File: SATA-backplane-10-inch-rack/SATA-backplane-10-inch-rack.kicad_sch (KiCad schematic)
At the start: 19 parts, among them J101 Conn_01x06, Q101 DMG1012UW, Q102 DMG1012UW, U1 NCP1117-3.3_SOT223

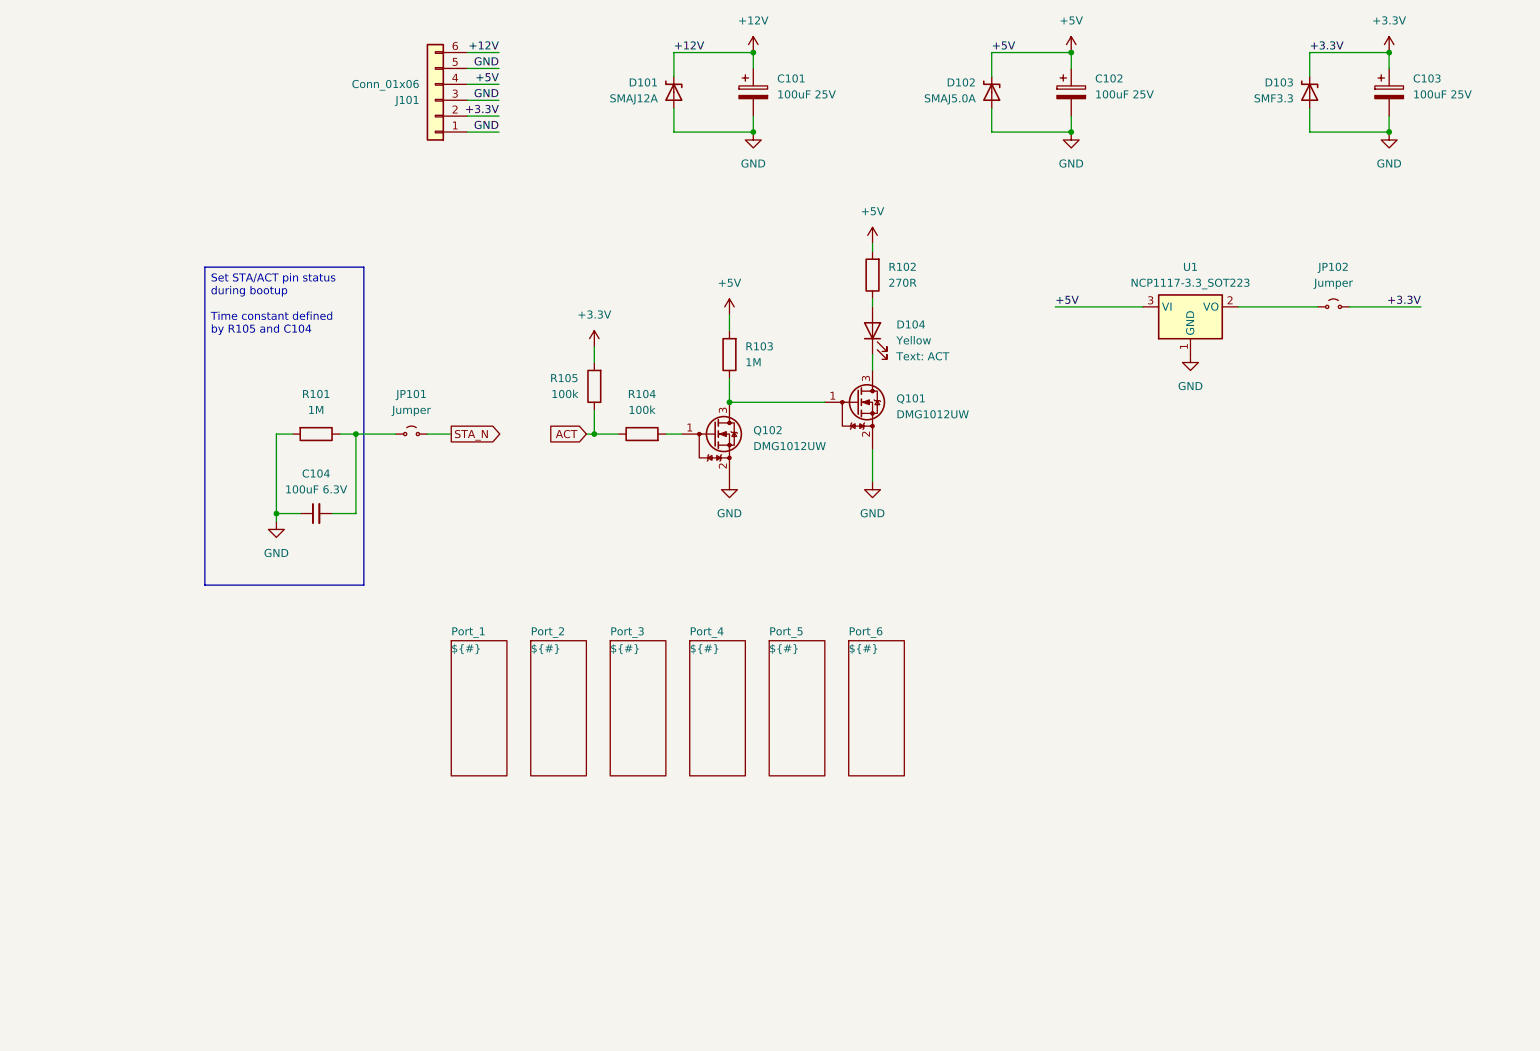
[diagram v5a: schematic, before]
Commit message: Rearrange reference designators numbering and silkscreen items
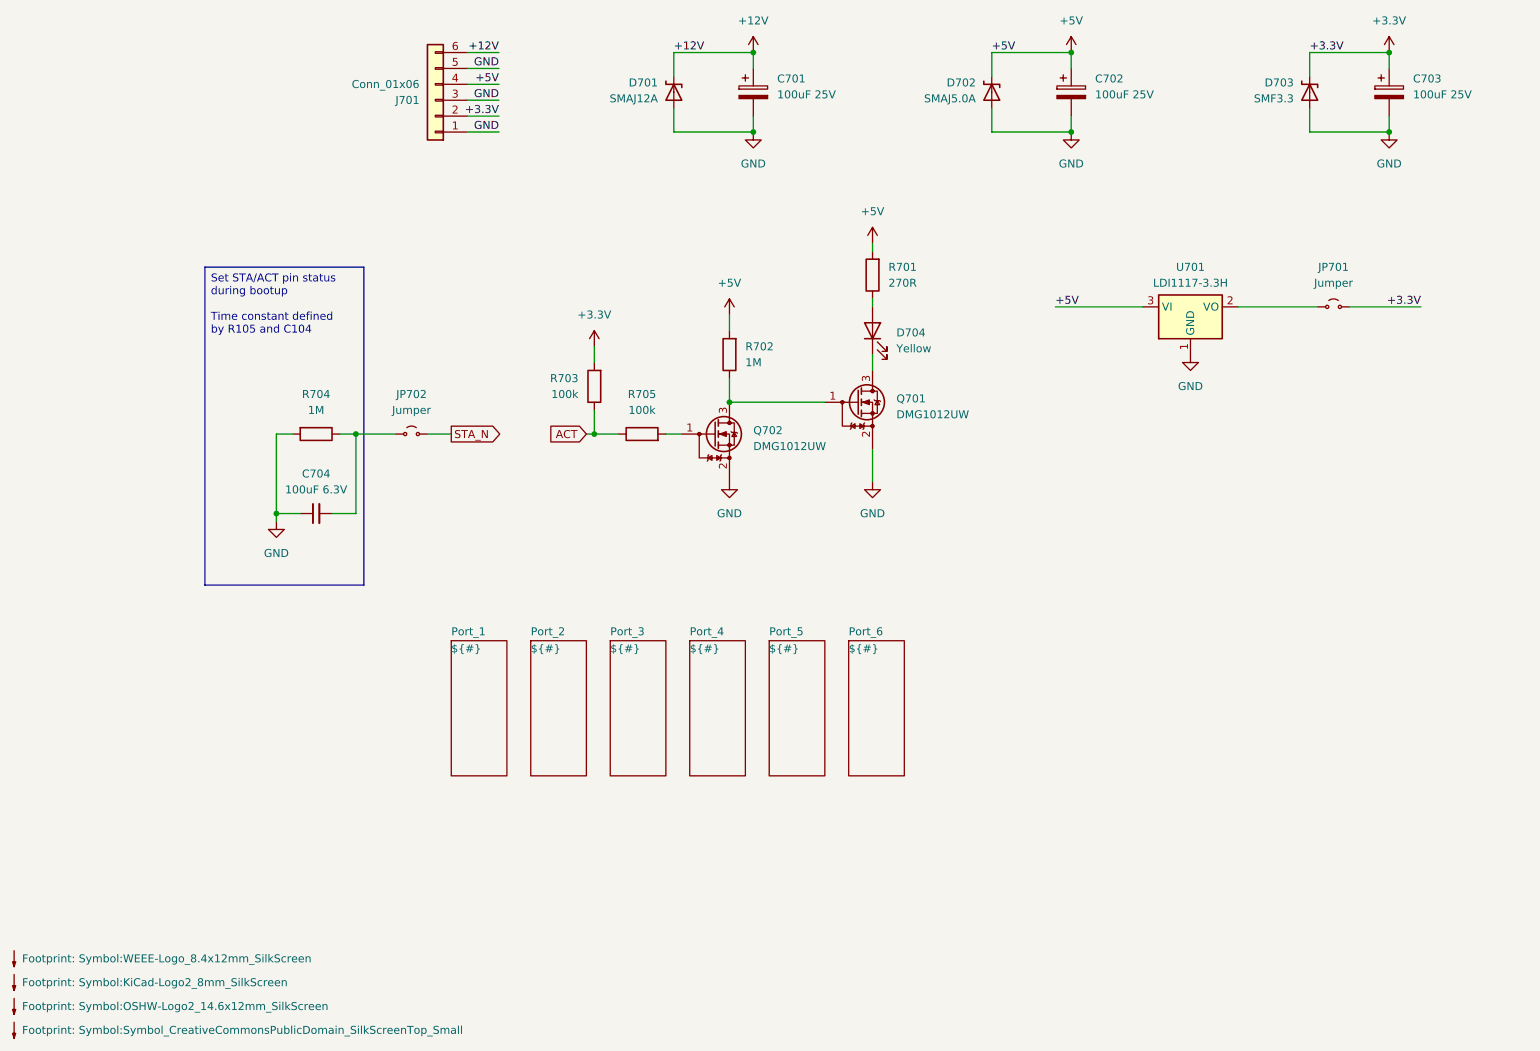
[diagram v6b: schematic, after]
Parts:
- added SYM701: ~, Symbol:Symbol_CreativeCommonsPublicDomain_SilkScreenTop_Small, symbol Graphic:SYM_Arrow_Tiny
- added SYM702: ~, Symbol:WEEE-Logo_8.4x12mm_SilkScreen, symbol Graphic:SYM_Arrow_Tiny
- added SYM704: ~, Symbol:OSHW-Logo2_14.6x12mm_SilkScreen, symbol Graphic:SYM_Arrow_Tiny
- added SYM705: ~, Symbol:KiCad-Logo2_8mm_SilkScreen, symbol Graphic:SYM_Arrow_Tiny
- C704: renamed from C104; Manufacturer_Name (none) -> Taiyo Yuden; Manufacturer_Part_Number 100uF 6.3V -> JMK325BJ107MM-T; Mouser Part Number (none) -> 963-JMK325BJ107MM-T
- D704: renamed from D104; Manufacturer_Part_Number Yellow led -> LTL-4251N; Mouser Part Number (none) -> 859-LTL-4251N; Text ACT -> (none)
- J701: renamed from J101; footprint TerminalBlock_Phoenix_PT-1,5-6-3.5-H_1x06_P3.50mm_Horizontal -> TerminalBlock_Phoenix:TerminalBlock_Phoenix_PT-1,5-6-3.5-H_1x06_P3.50mm_Horizontal
- JP701: renamed from JP102; Manufacturer_Part_Number PinHeader_1x02_P2.54mm_bended -> 22-28-8024; Mouser Part Number (none) -> 538-22-28-8024
- JP702: renamed from JP101; Manufacturer_Part_Number PinHeader_1x02_P2.54mm_bended -> 22-28-8024; Mouser Part Number (none) -> 538-22-28-8024
- R701: renamed from R102; Manufacturer_Part_Number 270R -> AC0805FR-07270RL; Mouser Part Number (none) -> 603-AC0805FR-07270RL
- R702: renamed from R103; Manufacturer_Part_Number 1M -> AC0805FR-071ML; Mouser Part Number (none) -> 603-AC0805FR-071ML
- R703: renamed from R105; Manufacturer_Part_Number 100k -> AC0805FR-07100KL; Mouser Part Number (none) -> 603-AC0805FR-07100KL
- R704: renamed from R101; Manufacturer_Part_Number 1M -> AC0805FR-071ML; Mouser Part Number (none) -> 603-AC0805FR-071ML
- R705: renamed from R104; Manufacturer_Part_Number 100k -> AC0805FR-07100KL; Mouser Part Number (none) -> 603-AC0805FR-07100KL
- U701: renamed from U1; value NCP1117-3.3_SOT223 -> LDI1117-3.3H; Manufacturer_Part_Number NCP1117-3.3_SOT223 -> LDI1117-3.3H; Mouser Part Number (none) -> 637-LDI1117-3.3H
- renumbered C101 to C701, C102 to C702, C103 to C703, D101 to D701, D102 to D702, D103 to D703, Q101 to Q701, Q102 to Q702
